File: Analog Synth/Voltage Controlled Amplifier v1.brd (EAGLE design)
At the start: 100 x 100 mm, 45 parts, among them IC1 TL084P, IC2 TL084P, IC3 TL084P, IC4 CA3046, IC5 78L05Z, IC6 79L05

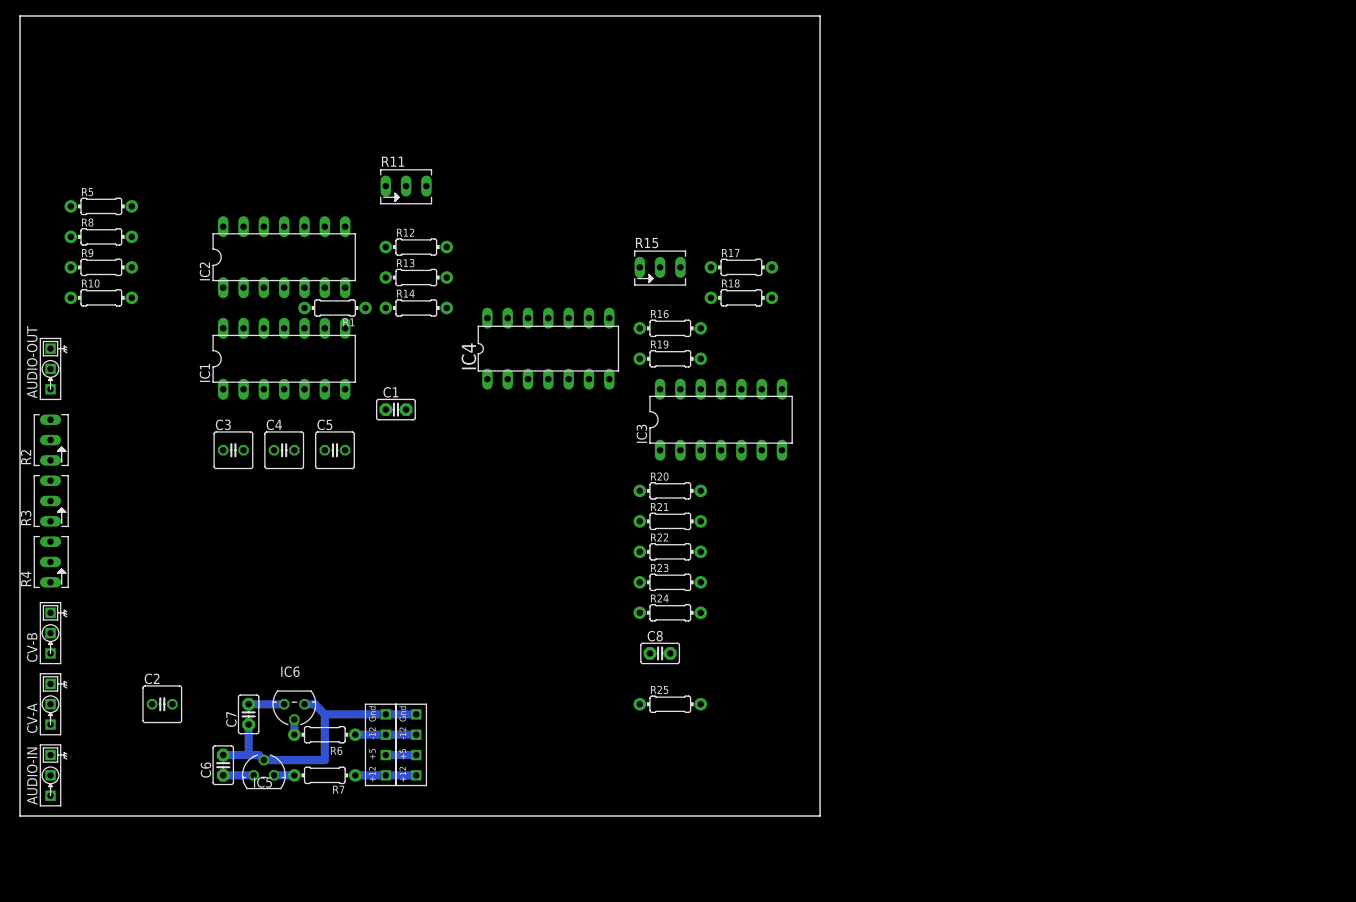
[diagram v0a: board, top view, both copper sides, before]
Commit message: working on VCA-v1
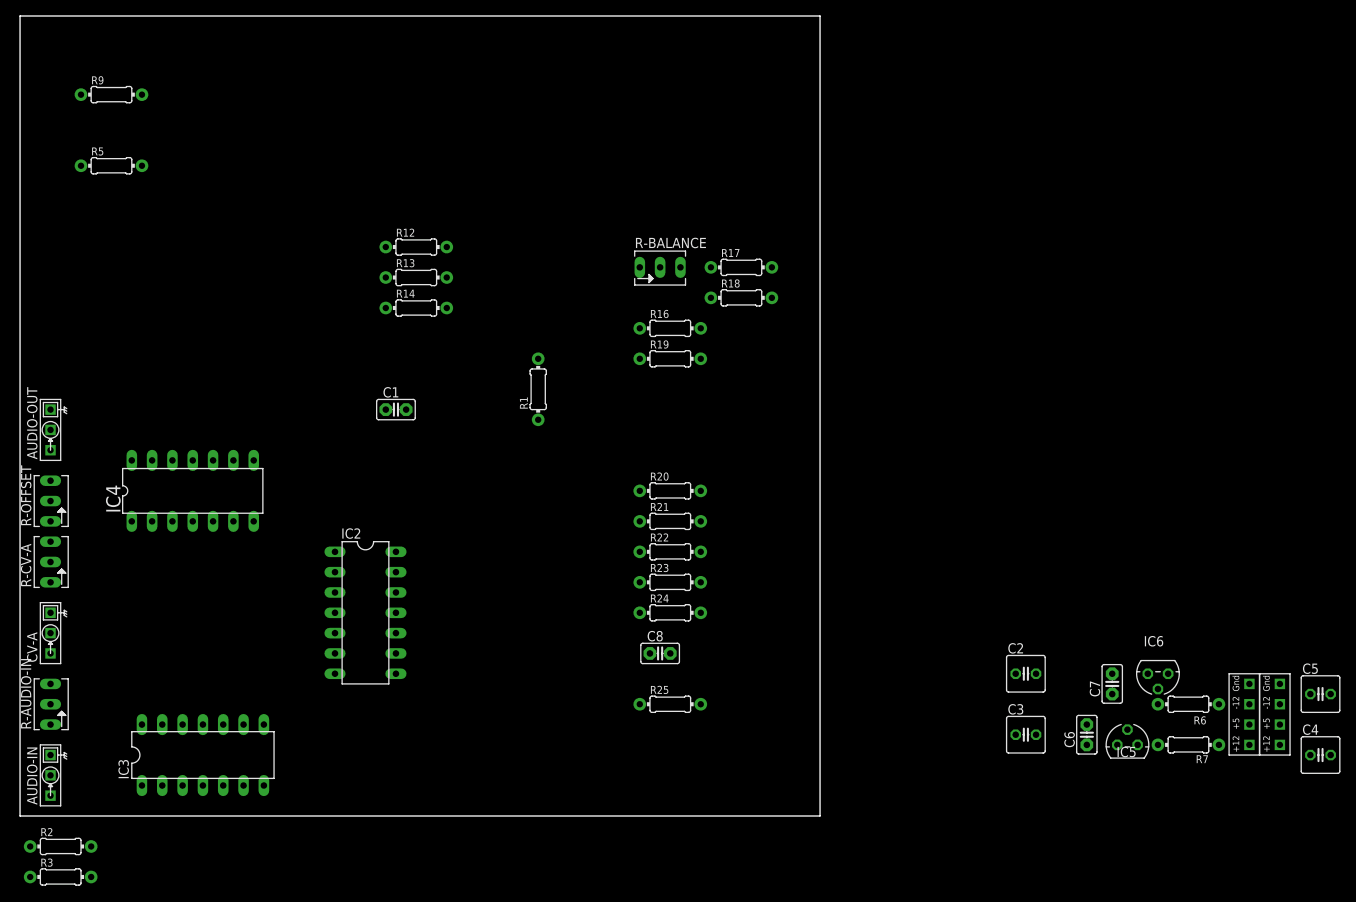
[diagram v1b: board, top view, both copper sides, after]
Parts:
- removed CV-B: I/O, !synth_sch:MONO_JACK
- removed IC1: TL084P, linear:DIL14
- removed R10: 2.7k, resistor:0204/7
- removed R11: 100k Log, pot:B64Y
- removed R8: 100k, resistor:0204/7
- added R-AUDIO-IN: 100k Log, pot:B64Y
- added R-OFFSET: 10k Lin, pot:B64Y
- R-CV-A: value 10k Lin -> 100k Log
- R2, R3: value 100k Log -> 100k; device pot:B64Y -> resistor:0204/7
- moved C4 135.0 mm to (162.6, 7.62)
- moved C5 126.9 mm to (162.6, 15.2)
- moved IC6 108.0 mm to (142.2, 17.8)
- moved R6 108.0 mm to (146.1, 14.0)
- moved R7 108.0 mm to (146.1, 8.89)
- moved C2 108.0 mm to (125.7, 17.8)
- moved C7 108.0 mm to (136.5, 16.5)
- moved IC5 108.0 mm to (138.4, 8.89)
- moved C6 108.0 mm to (133.3, 10.2)
- moved U$3 108.0 mm to (153.7, 12.7)
- moved U$7 108.0 mm to (157.5, 12.7)
- moved C3 105.2 mm to (125.7, 10.2)
- moved IC3 77.1 mm to (22.9, 7.62)
- moved R2 50.8 mm to (5.08, -3.81), turned to 0 degrees
- moved IC4 47.9 mm to (21.6, 40.6)
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- renumbered R15 to R-BALANCE, R4 to R-CV-A
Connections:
- removed net N$35: IC3.8, IC3.9
- removed net N$36: IC3.13, IC3.14
- removed net N$8: IC1.12, R2.S
- removed net N$9: IC1.13, IC1.14, R8.1
- net -5V-REG: now also R-OFFSET.A; no longer R-CV-A.A
- net 5V-REG: now also R-OFFSET.E; no longer R-CV-A.E
- net GND: now also R-AUDIO-IN.A, R-CV-A.A; no longer CV-B.P$1, CV-B.P$3, IC3.10, IC3.12, R11.A, R2.A, R3.A
- net N$1: now also IC3.13, IC3.14; no longer IC1.6, IC1.7
- net N$13: now also R-OFFSET.S
- net N$14: now also IC3.12, R-CV-A.S; no longer IC1.5, R3.S
- net N$15: now also R2.1; no longer R-BALANCE.A, R10.2
- net N$16: no longer R10.1
- net N$19: now also R-AUDIO-IN.S; no longer R11.S
- net N$20: now also R-AUDIO-IN.E; no longer R11.E
- net N$23: now also R3.2; no longer R-BALANCE.E
- net N$3: now also IC3.10; no longer IC1.3
- net N$4: now also IC3.8, IC3.9, R-CV-A.E; no longer IC1.1, IC1.2, R3.E
- net N$5: now also R-BALANCE.E, R3.1; no longer CV-B.P$2, IC1.10
- net N$6: no longer R8.2
- net N$7: now also R-BALANCE.A, R2.2; no longer IC1.8, IC1.9, R2.E
- net V+: no longer IC1.4
- net V-: no longer IC1.11
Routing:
- net GND: track 37.0 -> 0.00 mm
- net N$12: track 7.62 -> 0.00 mm
- net N$10: track 7.62 -> 0.00 mm
- net -5V-REG: track 4.45 -> 0.00 mm
- net N$11: track 3.81 -> 0.00 mm
- net 5V-REG: track 3.81 -> 0.00 mm
- net +12V: track 2.54 -> 0.00 mm
- net -12V: track 1.90 -> 0.00 mm

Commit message: Working on Power Distribution Board
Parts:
- moved R3 115.3 mm to (80.0, 80.0)
- moved R2 108.7 mm to (80.0, 74.9)
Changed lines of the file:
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@@
 <element name="R25" library="resistor" package="0204/7" value="1k" x="81.28" y="13.97"/>
 <element name="AUDIO-OUT" library="!synth_sch" package="MONO_JACK" value="I/O" x="3.81" y="48.26" rot="R90"/>
-<element name="R2" library="resistor" package="0204/7" value="100k" x="5.08" y="-3.81"/>
-<element name="R3" library="resistor" package="0204/7" value="100k" x="5.08" y="-7.62"/>
+<element name="R2" library="resistor" package="0204/7" value="100k" x="80.01" y="74.93"/>
+<element name="R3" library="resistor" package="0204/7" value="100k" x="80.01" y="80.01"/>
 </elements>
 <signals>
@@
 <contactref element="R2" pad="1"/>
 <wire x1="39.37" y1="17.78" x2="53.34" y2="63.5" width="0" layer="19" extent="1-1"/>
-<wire x1="1.27" y1="-3.81" x2="39.37" y2="17.78" width="0" layer="19" extent="1-1"/>
+<wire x1="76.2" y1="74.93" x2="39.37" y2="17.78" width="0" layer="19" extent="1-1"/>
 </signal>
 <signal name="N$16">
@@
 <contactref element="R3" pad="2"/>
 <wire x1="46.99" y1="17.78" x2="86.36" y2="68.58" width="0" layer="19" extent="1-1"/>
-<wire x1="8.89" y1="-7.62" x2="46.99" y2="17.78" width="0" layer="19" extent="1-1"/>
+<wire x1="83.82" y1="80.01" x2="46.99" y2="17.78" width="0" layer="19" extent="1-1"/>
 </signal>
 <signal name="N$2">
@@
 <contactref element="R3" pad="1"/>
 <contactref element="R-BALANCE" pad="E"/>
-<wire x1="1.27" y1="-7.62" x2="77.47" y2="68.58" width="0" layer="19" extent="1-1"/>
+<wire x1="76.2" y1="80.01" x2="77.47" y2="68.58" width="0" layer="19" extent="1-1"/>
 </signal>
 <signal name="N$7">
 <contactref element="R-BALANCE" pad="A"/>
 <contactref element="R2" pad="2"/>
-<wire x1="8.89" y1="-3.81" x2="82.55" y2="68.58" width="0" layer="19" extent="1-1"/>
+<wire x1="83.82" y1="74.93" x2="82.55" y2="68.58" width="0" layer="19" extent="1-1"/>
 </signal>
 </signals>

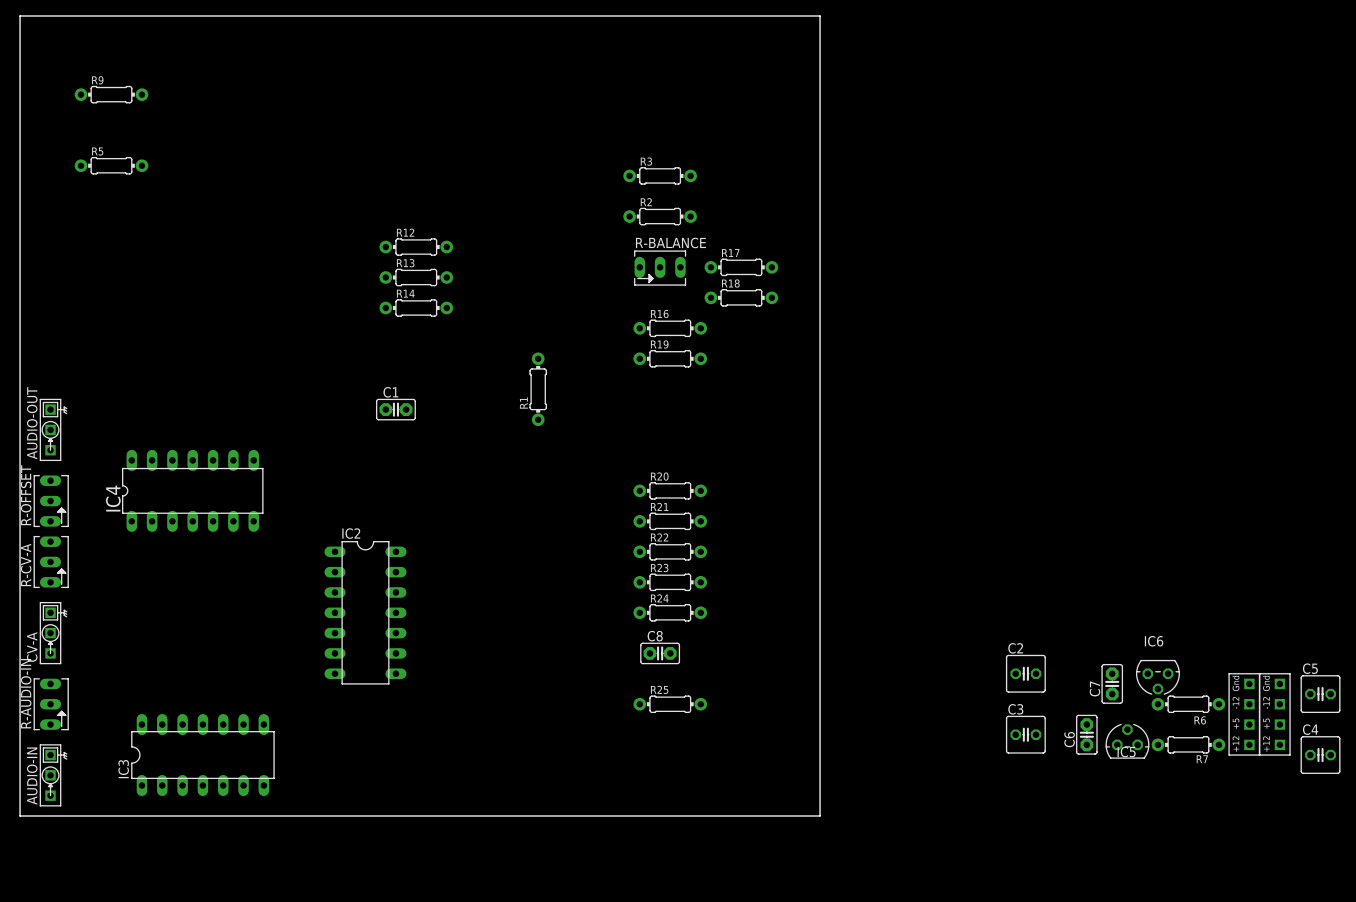
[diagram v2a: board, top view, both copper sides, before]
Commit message: working on Power Distribution and VCA.
When playing with my VCA on my bench, I discovered it can be used as an AM radio to pick up a local station on 1420 kHz (KTOE in Mankato)
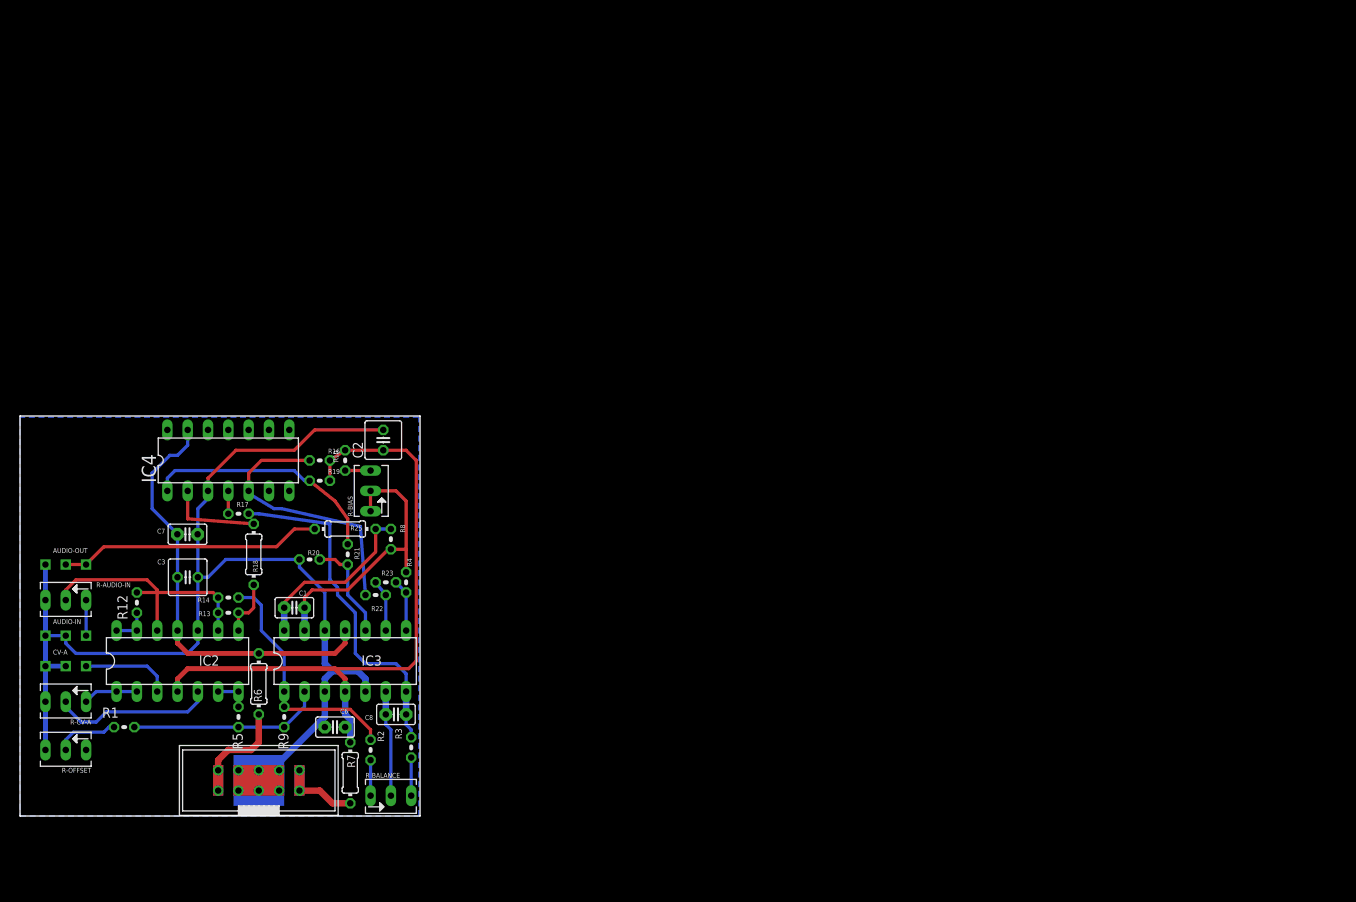
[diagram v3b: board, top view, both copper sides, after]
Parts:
- removed C4, C5: 10µ, rcl:C025-050X050
- removed IC5: 78L05Z, linear:TO92
- removed IC6: 79L05, linear:TO92
- removed R24: 100k, resistor:0204/7
- removed U$3, U$7: POWER_CONNECTOR_4_RGBB, !synth_sch:POWER_CONNECTOR_4_RGBB
- added R-BIAS: 100k Trim, pot:B64Y
- added R10, R8: 10k, resistor:0204V
- added R4: 1k, resistor:0204V
- added U$1: EURORACK-POWER, !synth_sch:EURORACK-POWER
- C1, C8: value 1µ -> 471pf
- R1, R12, R13, R14, R16, R17, R19, R2, R20, R21, R22, R23, R3, R5: device resistor:0204/7 -> resistor:0204V
- R9: value 27k -> 33k; device resistor:0204/7 -> resistor:0204V
- moved C7 117.1 mm to (20.9, 35.2), turned to 180 degrees
- moved R6 116.2 mm to (29.8, 16.5), turned to 270 degrees
- moved C3 106.6 mm to (21.0, 29.8), turned to 180 degrees
- moved R7 104.8 mm to (41.3, 5.40), turned to 90 degrees
- moved C6 94.0 mm to (39.4, 11.1), turned to 180 degrees
- moved C2 85.5 mm to (45.4, 47.0), turned to 90 degrees
- moved R9 80.7 mm to (33.0, 12.4), turned to 270 degrees
- moved R3 77.9 mm to (48.9, 8.57), turned to 90 degrees
- moved R2 75.9 mm to (43.8, 8.26), turned to 270 degrees
- moved R-BALANCE 74.1 mm to (46.4, 2.54)
- moved R5 70.7 mm to (27.3, 12.4), turned to 270 degrees
- moved R17 70.0 mm to (27.3, 37.8)
- moved R18 68.9 mm to (29.2, 32.7), turned to 270 degrees
- moved R1 66.8 mm to (13.0, 11.1), turned to 0 degrees
- moved R12 56.5 mm to (14.6, 26.7), turned to 90 degrees
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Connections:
- removed net -5V-REG: C5.2, C7.2, IC6.3, R-OFFSET.A
- removed net N$11: U$3.+5, U$7.+5
- removed net N$12: R6.2, U$3.-12, U$7.-12
- removed net N$17: AUDIO-IN.P$2, C1.1
- removed net N$29: C8.2, IC3.5, R24.2
- removed net V+: IC2.4, IC3.4
- removed net V-: IC2.11, IC3.11
- new net N$8: R6.2, U$1.P$10, U$1.P$9
- new net N$9: AUDIO-IN.P$2, R-AUDIO-IN.E
- net +12V: now also C6.1, IC2.4, IC3.4, R10.2; no longer IC5.3
- net -12V: now also C7.2, IC2.11, IC3.11; no longer IC4.10, IC4.11, IC4.12, IC4.14, IC4.6, IC4.7, IC4.8, IC4.9, IC6.2
- net 5V-REG: no longer C4.1, C6.1, IC5.1
- net GND: now also IC3.12, IC3.3, IC3.5, R-OFFSET.A, U$1.P$3, U$1.P$4, U$1.P$5, U$1.P$6, U$1.P$7, U$1.P$8; no longer C4.2, C5.1, IC2.3, IC2.5, IC5.2, IC6.1, R24.1, U$3.GND, U$7.GND
- net N$1: now also IC2.6, IC2.7; no longer IC3.13, IC3.14
- net N$10: now also U$1.P$1, U$1.P$2; no longer U$3.+12, U$7.+12
- net N$14: now also IC2.5; no longer IC3.12
- net N$15: now also IC3.1, R9.1; no longer IC2.7
- net N$16: now also R-BIAS.A, R10.1; no longer R9.2
- net N$2: now also IC4.4, R17.1; no longer IC4.2, R17.2
- net N$20: now also C1.1, IC3.13, R-BIAS.E, R-BIAS.S, R4.2, R8.2; no longer C1.2, R-AUDIO-IN.E
- net N$21: now also IC4.2; no longer IC4.4
- net N$22: now also IC2.9; no longer IC2.2
- net N$23: now also C8.2, IC3.7, R17.2; no longer IC2.8, R17.1
- net N$24: now also IC4.5; no longer IC4.1
- net N$25: now also C8.1, IC3.6; no longer IC2.9
- net N$26: now also IC4.1; no longer IC4.5
- net N$27: now also IC2.8; no longer IC2.1
- net N$28: now also IC3.10; no longer IC3.3
- net N$3: now also IC2.3; no longer IC3.10
- net N$30: now also IC3.9; no longer IC3.2
- net N$31: now also IC3.8, R4.1; no longer C8.1, IC3.1
- net N$34: now also C1.2, IC3.14, R8.1; no longer IC3.6, IC3.7
- net N$4: now also IC2.1, IC2.2; no longer IC3.8, IC3.9
- net N$5: now also R2.2; no longer R3.1
- net N$6: now also IC3.2, R9.2; no longer IC2.6, R9.1
- net N$7: now also R3.1; no longer R2.2
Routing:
- net GND: track 0.00 -> 175.3 mm
- net +12V: track 0.00 -> 82.6 mm
- net -12V: track 0.00 -> 54.8 mm
- net N$23: track 0.00 -> 43.4 mm
- net N$20: track 0.00 -> 35.7 mm
- net N$24: track 0.00 -> 34.2 mm
- net N$32: track 0.00 -> 33.0 mm
- net N$15: track 0.00 -> 30.4 mm
- net N$26: track 0.00 -> 30.3 mm
- net N$6: track 0.00 -> 24.2 mm
- net N$34: track 0.00 -> 22.3 mm
- net N$14: track 0.00 -> 20.3 mm
- net N$19: track 0.00 -> 18.8 mm
- net N$22: track 0.00 -> 14.6 mm
- net N$8: track 0.00 -> 13.3 mm
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- added copper zone on layer 16, net GND
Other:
- board size 100 x 100 mm -> 50 x 50 mm
